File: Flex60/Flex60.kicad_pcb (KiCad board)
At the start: 2 copper layers, 285 x 94.6 mm, 111 parts

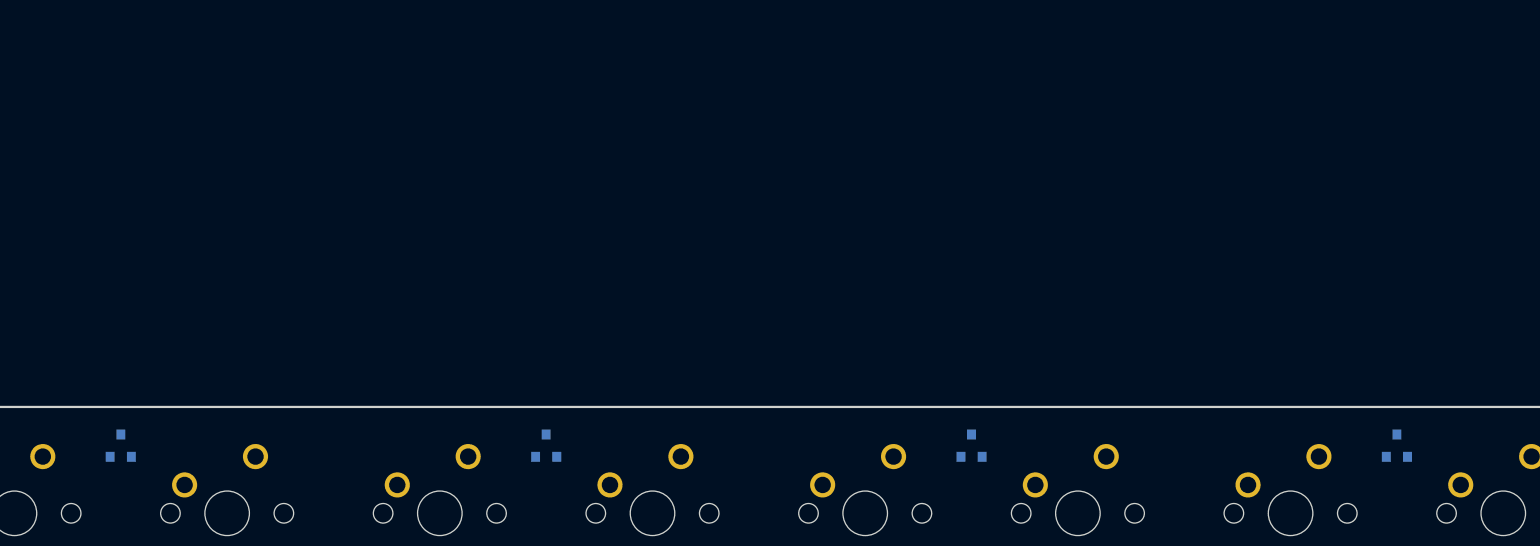
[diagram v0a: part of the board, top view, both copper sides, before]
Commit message: Add Footprints + 3D models
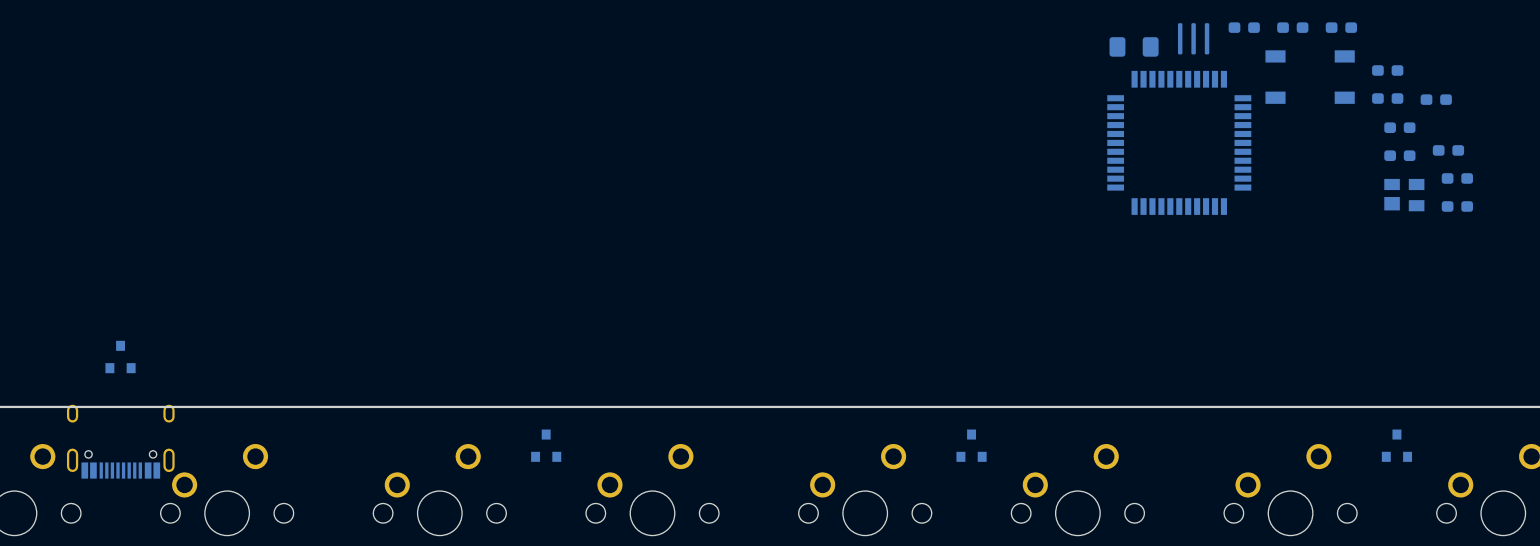
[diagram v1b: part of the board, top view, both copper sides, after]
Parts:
- added C1: 10µF, Custom_Footprints:C_0603_Annotated, B.Cu at (117.0, -41.0)
- added C2: 100nF, Custom_Footprints:C_0603_Annotated, B.Cu at (112.7, -41.0)
- added C3: 100nF, Custom_Footprints:C_0603_Annotated, B.Cu at (126.6, -29.5)
- added C4: 100nF, Custom_Footprints:C_0603_Annotated, B.Cu at (125.5, -34.6)
- added C5: 1µF, Custom_Footprints:C_0603_Annotated, B.Cu at (126.6, -32.0)
- added ESD1: PRTR5V0U2X, Package_TO_SOT_SMD:SOT-143, B.Cu at (127.0, -26.0)
- added F1: 500mA, Custom_Footprints:Fuse_1206_Annotated, B.Cu at (102.8, -39.2)
- added R1: 10kΩ, Custom_Footprints:R_0603_Annotated, B.Cu at (131.8, -27.5)
- added R2: 10kΩ, Custom_Footprints:R_0603_Annotated, B.Cu at (131.8, -25.0)
- added R3: 22Ω, Custom_Footprints:R_0603_Annotated, B.Cu at (125.5, -37.1)
- added R4: 22Ω, Custom_Footprints:R_0603_Annotated, B.Cu at (121.4, -41.0)
- added R5: 5.1kΩ, Custom_Footprints:R_0603_Annotated, B.Cu at (131.0, -30.0)
- added R6: 5.1kΩ, Custom_Footprints:R_0603_Annotated, B.Cu at (129.9, -34.5)
- added SW1: RESET, Custom_Footprints:Tactile_Switch, B.Cu at (118.6, -36.5)
- added U1: ATmega32U4-AU, Custom_Footprints:ATMEGA32U4_Annotated, B.Cu at (106.9, -30.6)
- added USB1: HRO-TYPE-C-31-M-12, Type-C:HRO-TYPE-C-31-M-12, B.Cu at (12.1, -9.00)
- added Y1: 16MHz, Custom_Footprints:Resonator_3Pin_Annotated, B.Cu at (108.1, -40.0)
- moved D1 7.94 mm to (12.0, -11.5)

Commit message: MCU placement
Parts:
- SW1: footprint Custom_Footprints:Tactile_Switch -> Custom_Footprints:RESET_PADS
- moved R3 141.6 mm to (-0.97, 26.4), turned to 90 degrees
- moved R4 141.4 mm to (-2.88, 26.4), turned to 90 degrees
- moved C4 132.4 mm to (18.6, 43.4), turned to 225 degrees
- moved R5 128.5 mm to (7.38, 5.03)
- moved C1 127.9 mm to (11.8, 31.6), turned to 180 degrees
- moved C5 126.4 mm to (15.5, 28.2), turned to 135 degrees
- moved R2 126.3 mm to (25.4, 43.1), turned to 135 degrees
- moved R6 119.6 mm to (17.0, 4.97), turned to 180 degrees
- moved ESD1 119.4 mm to (12.0, 6.03)
- moved R1 115.9 mm to (32.0, 31.5)
- moved C3 114.4 mm to (26.3, 25.4), turned to 45 degrees
- moved C2 110.4 mm to (32.0, 34.4)
- moved U1 106.7 mm to (22.2, 34.2), turned to 315 degrees
- moved SW1 105.5 mm to (37.9, 31.5), turned to 180 degrees
- moved Y1 104.4 mm to (28.3, 27.4), turned to 135 degrees
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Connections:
- ESD1 pad 2: DA+ -> DB-
- ESD1 pad 3: DA- -> DB+
- K_200 pad 2: Net-(D15-Pad2) -> Net-(D15-Pad1)
- K_200A1 pad 2: Net-(D15-Pad2) -> Net-(D15-Pad1)
- K_201 pad 2: Net-(D15-Pad1) -> Net-(D15-Pad2)
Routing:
- net row4: track 0.00 -> 236.0 mm
- net row1: track 0.00 -> 235.3 mm
- net row3: track 0.00 -> 226.7 mm
- net row0: track 0.00 -> 221.4 mm
- net row2: track 0.00 -> 198.0 mm
- net col0: track 0.00 -> 92.9 mm
- net +5V: track 0.00 -> 86.2 mm, vias 0 -> 6
- net Net-(D21-Pad1): track 0.00 -> 46.2 mm
- net DB+: track 0.00 -> 45.0 mm
- net Net-(D30-Pad1): track 0.00 -> 41.3 mm
- net Net-(D30-Pad2): track 0.00 -> 40.2 mm
- net DB-: track 0.00 -> 40.0 mm
- net col13: track 0.00 -> 39.9 mm
- net Net-(D27-Pad1): track 0.00 -> 27.8 mm
- net GND: track 0.00 -> 27.5 mm, vias 0 -> 8
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- added copper zone on B.Cu, net GND
- added copper zone on F.Cu, net GND

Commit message: Route Cols
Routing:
- net col6: track 21.0 -> 480.8 mm
- net col8: track 21.0 -> 354.0 mm
- net col9: track 21.0 -> 278.8 mm
- net col7: track 21.0 -> 269.7 mm
- net col5: track 21.0 -> 214.5 mm
- net col10: track 21.0 -> 203.6 mm
- net col4: track 21.0 -> 177.2 mm
- net col2: track 21.0 -> 172.0 mm
- net col11: track 21.0 -> 168.9 mm
- net col3: track 21.0 -> 139.8 mm
- net col12: track 0.00 -> 100.1 mm
- net col1: track 0.00 -> 58.6 mm
- net GND: track 27.5 -> 62.8 mm
- net Net-(R1-Pad2): track 3.76 -> 21.0 mm
- net col0: track 92.9 -> 91.9 mm

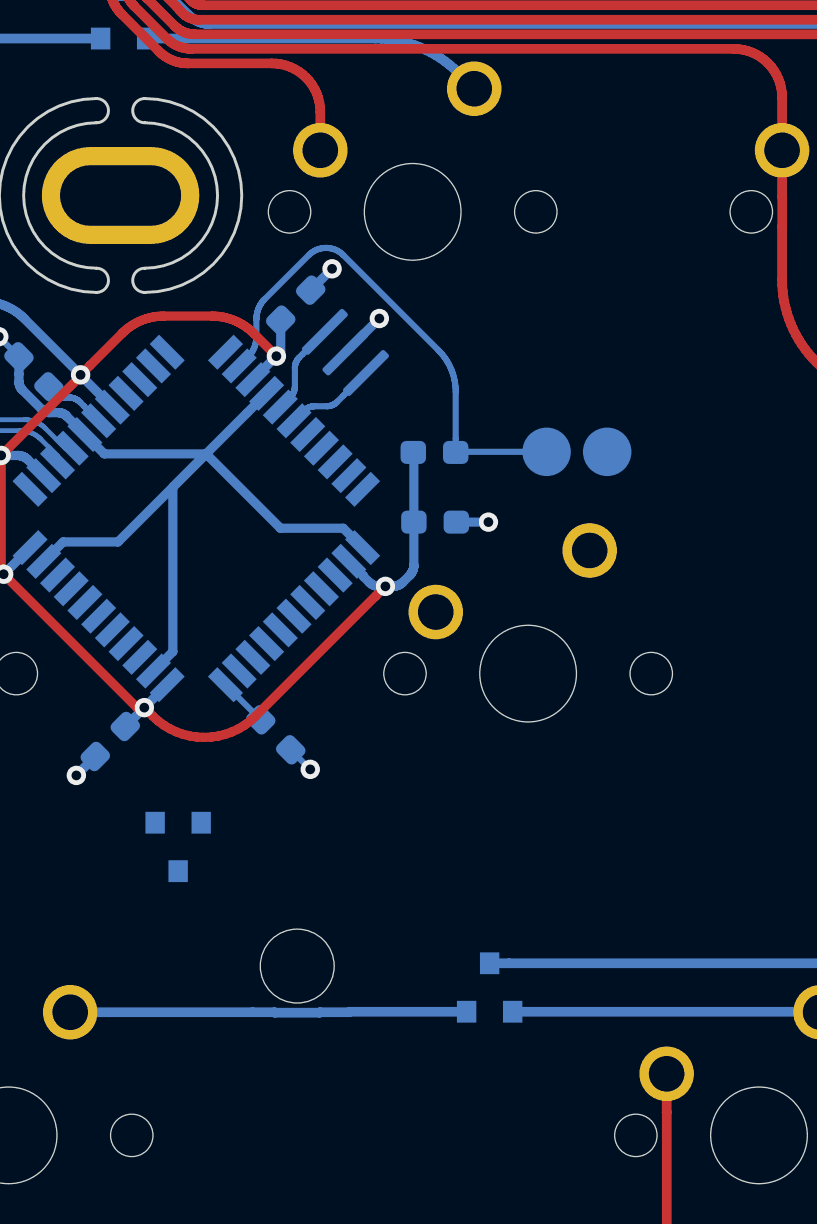
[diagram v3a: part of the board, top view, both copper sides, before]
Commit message: Change reset pads
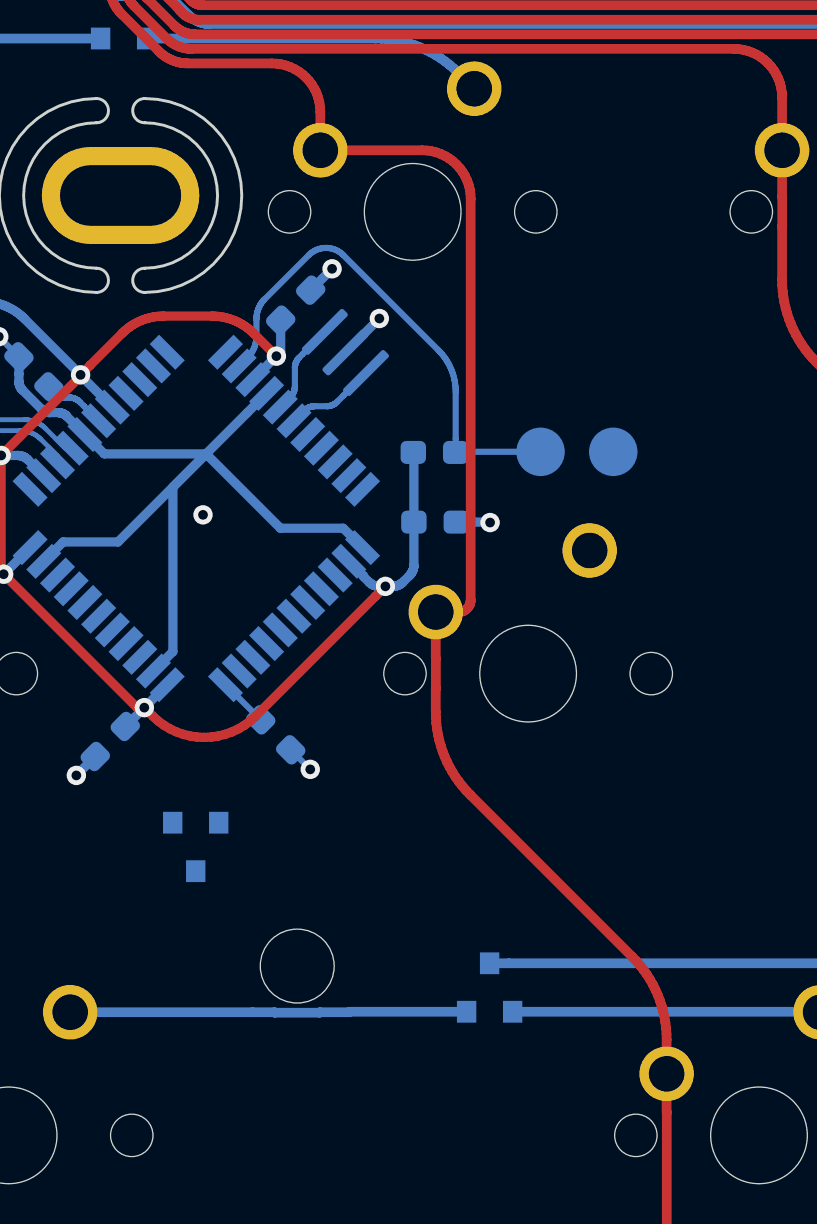
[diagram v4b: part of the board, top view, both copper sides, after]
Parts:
- moved D15 0.72 mm to (22.1, 47.8)
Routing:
- net col1: track 58.6 -> 106.9 mm
- net GND: vias 8 -> 9

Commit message: Route Matrix
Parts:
- moved H2 0.52 mm to (277.2, 49.8)
- moved H5 0.52 mm to (184.0, 78.5)
- moved H6 0.52 mm to (253.5, 21.2)
- moved H1 0.52 mm to (-5.25, 49.9)
- moved USB1 0.52 mm to (11.7, -8.68)
- moved H3 0.52 mm to (18.7, 21.2)
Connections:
- U1 pad 11: Net-(U1-Pad11) -> row1
- U1 pad 12: Net-(U1-Pad12) -> col1
- U1 pad 18: Net-(U1-Pad18) -> col13
- U1 pad 19: Net-(U1-Pad19) -> col12
- U1 pad 20: Net-(U1-Pad20) -> col11
- U1 pad 21: Net-(U1-Pad21) -> col10
- U1 pad 22: Net-(U1-Pad22) -> col9
- U1 pad 26: Net-(U1-Pad26) -> col8
- U1 pad 27: Net-(U1-Pad27) -> col7
- U1 pad 28: Net-(U1-Pad28) -> col6
- U1 pad 29: Net-(U1-Pad29) -> col5
- U1 pad 30: Net-(U1-Pad30) -> col4
- U1 pad 31: Net-(U1-Pad31) -> col3
- U1 pad 32: Net-(U1-Pad32) -> col2
- U1 pad 38: Net-(U1-Pad38) -> row2
- U1 pad 39: Net-(U1-Pad39) -> row3
- U1 pad 40: Net-(U1-Pad40) -> row4
- U1 pad 41: Net-(U1-Pad41) -> col0
- U1 pad 8: Net-(U1-Pad8) -> row0
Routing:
- net col13: track 39.9 -> 281.4 mm
- net col12: track 100.1 -> 312.2 mm, vias 0 -> 1
- net col11: track 168.9 -> 361.6 mm, vias 0 -> 1
- net col10: track 203.6 -> 376.9 mm, vias 0 -> 1
- net col9: track 278.8 -> 433.2 mm, vias 0 -> 3
- net col8: track 354.0 -> 497.1 mm, vias 0 -> 1
- net col7: track 269.7 -> 394.1 mm, vias 0 -> 1
- net col6: track 480.8 -> 586.6 mm, vias 0 -> 1
- net col5: track 214.5 -> 300.7 mm, vias 0 -> 1
- net row2: track 198.0 -> 270.2 mm, vias 0 -> 2
- net col4: track 177.2 -> 245.3 mm, vias 0 -> 1
- net col3: track 139.8 -> 189.8 mm, vias 0 -> 1
- net row0: track 221.4 -> 270.5 mm
- net row4: track 236.0 -> 279.2 mm
- net col2: track 172.0 -> 204.2 mm, vias 0 -> 1
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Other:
- outline, holes or cut-outs redrawn

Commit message: Fix routing
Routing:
- net col8: track 497.1 -> 500.9 mm, vias 1 -> 0
